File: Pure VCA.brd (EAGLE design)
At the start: 18.3 x 100 mm, 35 parts, among them U1 DUAL_OPAMP, U2 THAT_2181_SMD

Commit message: VCA 2.2
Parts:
- removed U1: DUAL_OPAMP, INSTRUO:DUAL_OPAMP
- removed U2: THAT_2181_SMD, INSTRUO:SOIC--8
- added IC1: TL072, GMSN:SO08
- added IC2: THAT2181, GMSN:SOIC--8
- BUSS: value (none) -> HEADER1X2PTH; device SparkFun-Connectors:1X02 -> GMSN:1X02
- C1, C3: device rcl:C0805K -> GMSN:C0805
- C2, C4, C5: value 10u -> 10uF; device rcl:153CLV-0505 -> GMSN:153CLV-0505
- C6, C7, C8, C9: value 0.1u -> 100nF; device rcl:C0805K -> GMSN:C0805
- CV_IN, SIG_IN, SIG_OUT: value (none) -> PJ301M-12; device INSTRUO:S_JACK -> GMSN:PJ301M-12
- CV_LEVEL, OFFSET: value 50K -> B100k; device INSTRUO:Q-POT -> GMSN:POTENTIOMETER_9MM
- D1, D2: value (none) -> STTH102A; device adafruit:SMADIODE -> GMSN:SMADIODE
- PWR: value (none) -> HEADER2X5SHD; device SparkFun-Connectors:2X5-SHROUDED -> GMSN:2X5-SHROUDED
- R1: value 47K -> 20k; device rcl:R0805 -> GMSN:R0805
- R10: value 220K* -> 130k; device rcl:R0805 -> GMSN:R0805
- R11, R5: device rcl:R0805 -> GMSN:R0805
- R12: value 19K1 -> 19k1; device rcl:R0805 -> GMSN:R0805
- R2: value 47K -> 2k2; device rcl:R0805 -> GMSN:R0805
- R3: value 47K -> 75k; device rcl:R0805 -> GMSN:R0805
- R4: value 13K -> 100R; device rcl:R0805 -> GMSN:R0805
- R6, R8: value 20K -> 20k; device rcl:R0805 -> GMSN:R0805
- R7: value 4K12 -> 4k12; device rcl:R0805 -> GMSN:R0805
- R9: value 1K -> 1k; device rcl:R0805 -> GMSN:R0805
- TR1: value 50K -> 50k; device INSTRUO:TRIM_3269W -> GMSN:TRIMMER_TH
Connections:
- removed net N$10: C2.-, R6.2
- net +12V: now also IC1.8, IC2.7; no longer U1.+VCC, U2.7
- net -12V: now also IC1.4; no longer U1.-VCC
- net GND: now also IC1.5, IC2.2, IC2.6; no longer U1.+2IN, U2.2, U2.6
- net N$11: now also C2.-, R6.2
- net N$13: now also IC2.5; no longer U2.5
- net N$14: now also IC1.3; no longer U1.+1IN
- net N$15: now also IC1.6, IC2.8; no longer U1.-2IN, U2.8
- net N$16: now also IC1.7; no longer U1.2OUT
- net N$17: now also IC2.4; no longer U2.4
- net N$2: now also IC1.2; no longer U1.-1IN
- net N$5: now also IC1.1, IC2.3; no longer U1.1OUT, U2.3
- net N$9: now also IC2.1; no longer U2.1
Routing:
- net N$10: track 5.22 -> 0.00 mm
- net N$11: track 19.9 -> 24.6 mm
- net +12V: track 111.4 -> 114.8 mm
- net N$18: track 16.3 -> 19.5 mm
- net GND: track 12.1 -> 9.93 mm
- net -12V: track 100.2 -> 101.2 mm
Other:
- board text added: "Pure VCA V2.2"
- board text added: "copyright GMSN Ltd 2016"
- board text removed: "Designed by Rob Spencer and Jason H. J. Lim copyright GMSN Ltd 2016"
- board text removed: "Pure VCA V2.1"

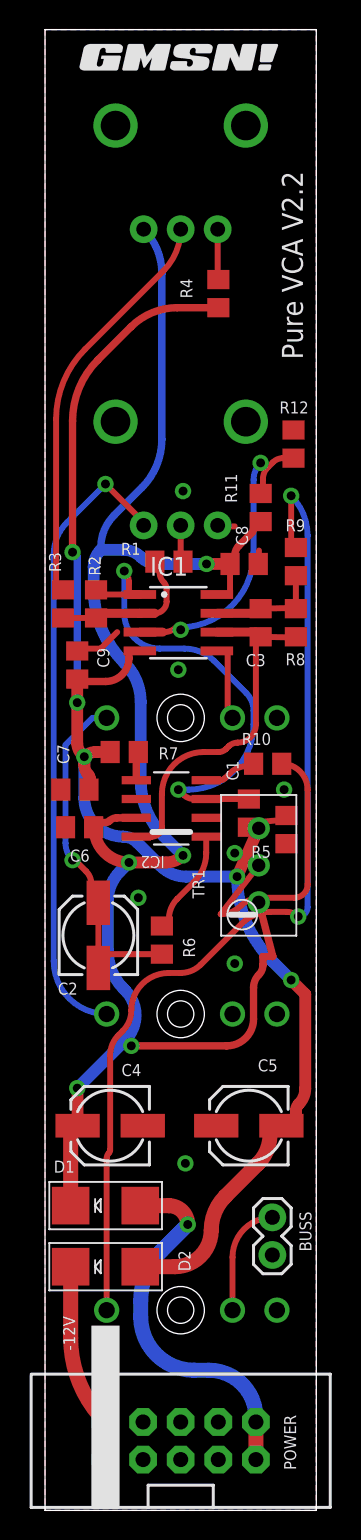
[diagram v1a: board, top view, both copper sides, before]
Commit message: VCA 2.3
VCA Updated to V2.3 14/4/21

Library updated to include 3D models.
Traces rerouted.
Weird shorted cap removed. WTF?
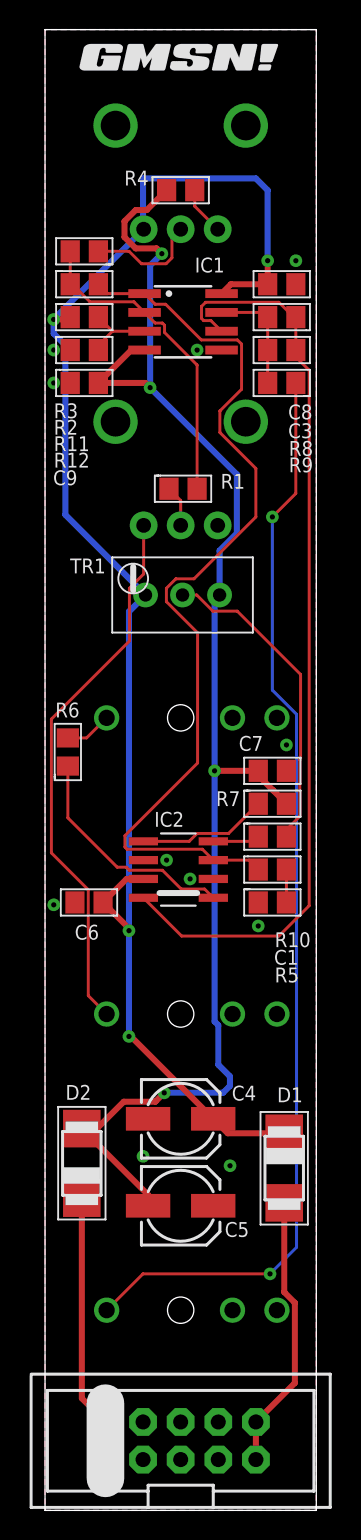
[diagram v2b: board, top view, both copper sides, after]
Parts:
- removed BUSS: HEADER1X2PTH, GMSN:1X02
- removed C2: 10uF, GMSN:153CLV-0505
- CV_LEVEL: device GMSN:POTENTIOMETER_9MM -> GMSN:POT_9MM_GREEN_KNOB
- OFFSET: device GMSN:POTENTIOMETER_9MM -> GMSN:POT_9MM_BLUE_KNOB
- moved R3 23.9 mm to (3.65, 101.8), turned to 180 degrees
- moved TR1 23.8 mm to (6.99, 79.7), turned to 180 degrees
- moved R2 21.6 mm to (3.65, 99.5), turned to 0 degrees
- moved C3 20.7 mm to (17.0, 97.3), turned to 180 degrees
- moved IC1 20.3 mm to (10.3, 97.0)
- moved C8 19.1 mm to (17.0, 99.5)
- moved C9 19.1 mm to (3.65, 92.9), turned to 0 degrees
- moved R8 18.4 mm to (17.0, 95.1), turned to 0 degrees
- moved R11 17.5 mm to (3.65, 97.3), turned to 0 degrees
- moved R12 15.5 mm to (3.65, 95.1), turned to 0 degrees
- moved U$2 15.4 mm to (9.68, 114.8)
- moved R6 14.2 mm to (2.54, 67.9), turned to 90 degrees
- moved C7 13.4 mm to (16.4, 66.7), turned to 180 degrees
- moved D1 12.3 mm to (17.2, 39.8), turned to 270 degrees
- moved R9 12.1 mm to (17.0, 92.9), turned to 180 degrees
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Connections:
- removed net N$12: BUSS.1, SIG_OUT.NORM
- net GND: now also CV_IN.NORM; no longer BUSS.2
- net N$11: no longer C2.+, C2.-
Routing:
- net N$15: track 24.4 -> 62.7 mm
- net N$5: track 32.2 -> 62.7 mm, vias 2 -> 0
- net N$11: track 24.6 -> 3.18 mm, vias 1 -> 0
- net N$6: track 27.5 -> 7.66 mm
- net N$14: track 20.6 -> 5.18 mm, vias 2 -> 0
- net +12V: track 114.8 -> 102.4 mm, vias 5 -> 4
- net N$2: track 11.4 -> 21.7 mm
- net GND: track 9.93 -> 0.00 mm, vias 7 -> 11
- net N$9: track 6.98 -> 15.6 mm
- net N$12: track 7.38 -> 0.00 mm
- net N$8: track 67.0 -> 74.3 mm
- net N$13: track 1.96 -> 8.81 mm
- net N$38: track 24.4 -> 18.7 mm, vias 1 -> 0
- net N$1: track 42.4 -> 37.1 mm, vias 1 -> 0
- net N$50: track 13.5 -> 18.3 mm
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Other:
- board text added: "Pure VCA V2.3 cc-by 4.0 2021 The Little Red Hen"
- board text removed: "-12V"
- board text removed: "CV_LEVEL"
- board text removed: "OFFSET"
- board text removed: "POWER"
- board text removed: "Pure VCA V2.2"
- board text removed: "copyright GMSN Ltd 2016"

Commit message: VCA 2.31
VCA Updated to V2.31 14/4/21

Library updated to include 3D models.
Traces rerouted.
Weird shorted cap removed. WTF?
Values tweaked for better CV response.
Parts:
- CV_LEVEL, OFFSET: value B100k -> B10k
- R1: value 20k -> 15k
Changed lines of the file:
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@@
 <drawing>
 <settings>
-<setting alwaysvectorfont="yes"/>
+<setting alwaysvectorfont="no"/>
 <setting keepoldvectorfont="yes"/>
 <setting verticaltext="up"/>
@@
 </autorouter>
 <elements>
-<element name="OFFSET" library="GMSN" library_urn="urn:adsk.eagle:library:27425118" package="POT_9MM_BLUE_KNOB" package3d_urn="urn:adsk.eagle:package:27948773/2" value="B100k" x="10.16" y="110.25" locked="yes" smashed="yes" rot="MR0">
+<element name="OFFSET" library="GMSN" library_urn="urn:adsk.eagle:library:27425118" package="POT_9MM_BLUE_KNOB" package3d_urn="urn:adsk.eagle:package:27948773/2" value="B10k" x="10.16" y="110.25" locked="yes" smashed="yes" rot="MR0">
 <attribute name="SORT" value="8" x="10.16" y="110.25" locked="yes" size="1.778" layer="28" rot="MR0" display="off"/>
 </element>
@@
 <attribute name="SORT" value="8" x="10.16" y="50.25" locked="yes" size="1.778" layer="28" rot="MR270" display="off"/>
 </element>
-<element name="CV_LEVEL" library="GMSN" library_urn="urn:adsk.eagle:library:27425118" package="POT_9MM_GREEN_KNOB" package3d_urn="urn:adsk.eagle:package:27948774/2" value="B100k" x="10.16" y="90.25" locked="yes" smashed="yes" rot="MR0">
+<element name="CV_LEVEL" library="GMSN" library_urn="urn:adsk.eagle:library:27425118" package="POT_9MM_GREEN_KNOB" package3d_urn="urn:adsk.eagle:package:27948774/2" value="B10k" x="10.16" y="90.25" locked="yes" smashed="yes" rot="MR0">
 <attribute name="SORT" value="8" x="10.16" y="90.25" locked="yes" size="1.778" layer="28" rot="MR0" display="off"/>
 </element>
@@
 <attribute name="VALUE" x="-0.254" y="18.51025" locked="yes" size="0.4064" layer="27" font="vector" rot="R90"/>
 </element>
-<element name="R1" library="GMSN" library_urn="urn:adsk.eagle:library:27425118" package="R0805" package3d_urn="urn:adsk.eagle:package:27425978/1" value="20k" x="10.31875" y="85.725" smashed="yes">
+<element name="R1" library="GMSN" library_urn="urn:adsk.eagle:library:27425118" package="R0805" package3d_urn="urn:adsk.eagle:package:27425978/1" value="15k" x="10.31875" y="85.725" smashed="yes">
 <attribute name="NAME" x="12.85875" y="85.725" size="1" layer="25" ratio="13"/>
 <attribute name="SORT" value="2" x="10.31875" y="85.725" size="1.778" layer="27" display="off"/>
